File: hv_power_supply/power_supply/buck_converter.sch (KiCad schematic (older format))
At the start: 9 parts, among them U1 TLF50211ELXUMA2

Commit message: hvps buck rev2
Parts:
- removed C_IN1: C_47uF, footprints:C_0805_OEM, symbol formula:C_47uF
- removed C_OUT1: C_10uF, footprints:C_0805_OEM, symbol formula:C_10uF
- removed DNP1, DNP2, DNP3: R_0, symbol Device:R
- removed D_Schottky1: 10BQ100, symbol Device:D_Schottky
- removed L_OUT1: L_10uH, symbol Device:L
- removed R1: R_47k, symbol formula:R_47k
- removed U1: TLF50211ELXUMA2, symbol formula:TLF50211ELXUMA2
- added C1, C_IN: C_1uF, footprints:C_0805_OEM, symbol formula:C_1uF
- added C_OUT: C_10uF, footprints:C_0805_OEM, symbol formula:C_10uF
- added R?: R_10K, footprints:R_0805_OEM, symbol formula:R_10K
- added U2: MAXM15464, symbol formula:MAXM15464
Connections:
- net labels added: V_IN(24V), V_OUT(5V)
- net labels removed: VCC, VS
- wire segments 36 -> 22
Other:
- note removed: "Input Cap 2"
- note removed: "Input Cap 3\n"
- note removed: "Input Inductor"

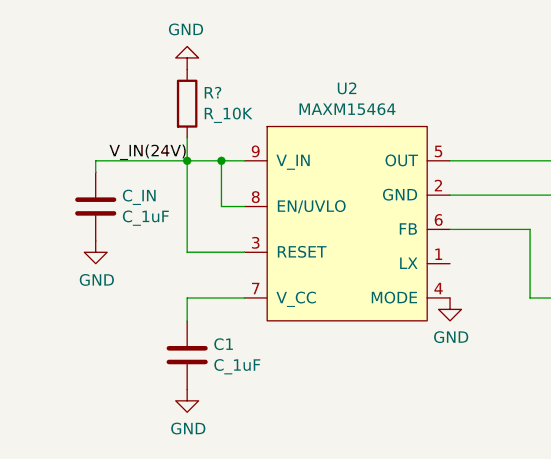
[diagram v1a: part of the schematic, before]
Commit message: buck with DNP part
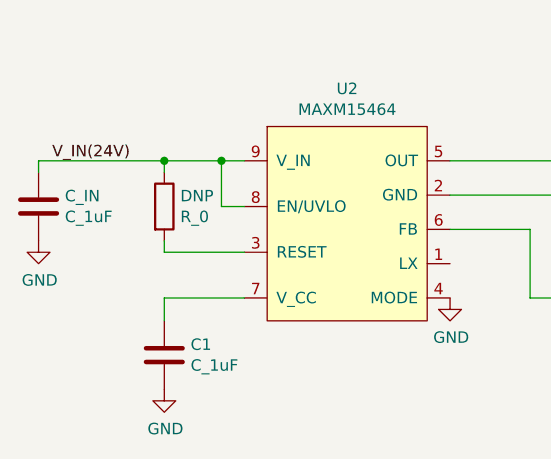
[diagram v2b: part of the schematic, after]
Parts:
- removed R?: R_10K, footprints:R_0805_OEM, symbol formula:R_10K
- added DNP: R_0, footprints:R_0603_1608Metric, symbol formula:R_0
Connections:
- net V_IN(24V): now also DNP.1; no longer U2.3 (RESET)
- new net: DNP.2, U2.3 (RESET)
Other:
- moved on the sheet: C1, C_IN
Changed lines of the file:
@@
 L formula:C_1uF C_IN
 U 1 1 60344498
-P 3700 3300
-F 0 "C_IN" H 3815 3396 50  0000 L CNN
-F 1 "C_1uF" H 3815 3305 50  0000 L CNN
-F 2 "footprints:C_0805_OEM" H 3738 3900 50  0001 C CNN
-F 3 "https://www.yageo.com/upload/media/product/productsearch/datasheet/mlcc/UPY-GPHC_Y5V_6.3V-to-50V_9.pdf" H 3725 4150 50  0001 C CNN
-F 4 "https://www.digikey.com/product-detail/en/yageo/CC0805ZKY5V9BB105/311-1909-1-ND/5195811#images" H 4125 3800 60  0001 C CNN "PurchasingLink"
-	1    3700 3300
+P 3450 3300
+F 0 "C_IN" H 3565 3396 50  0000 L CNN
+F 1 "C_1uF" H 3565 3305 50  0000 L CNN
+F 2 "footprints:C_0805_OEM" H 3488 3900 50  0001 C CNN
+F 3 "https://www.yageo.com/upload/media/product/productsearch/datasheet/mlcc/UPY-GPHC_Y5V_6.3V-to-50V_9.pdf" H 3475 4150 50  0001 C CNN
+F 4 "https://www.digikey.com/product-detail/en/yageo/CC0805ZKY5V9BB105/311-1909-1-ND/5195811#images" H 3875 3800 60  0001 C CNN "PurchasingLink"
+	1    3450 3300
 	1    0    0    -1
 $EndComp
@@
 L formula:C_1uF C1
 U 1 1 60347394
-P 4100 3950
-F 0 "C1" H 4215 4046 50  0000 L CNN
-F 1 "C_1uF" H 4215 3955 50  0000 L CNN
-F 2 "footprints:C_0805_OEM" H 4138 4550 50  0001 C CNN
-F 3 "https://www.yageo.com/upload/media/product/productsearch/datasheet/mlcc/UPY-GPHC_Y5V_6.3V-to-50V_9.pdf" H 4125 4800 50  0001 C CNN
-F 4 "https://www.digikey.com/product-detail/en/yageo/CC0805ZKY5V9BB105/311-1909-1-ND/5195811#images" H 4525 4450 60  0001 C CNN "PurchasingLink"
-	1    4100 3950
+P 4000 3950
+F 0 "C1" H 4115 4046 50  0000 L CNN
+F 1 "C_1uF" H 4115 3955 50  0000 L CNN
+F 2 "footprints:C_0805_OEM" H 4038 4550 50  0001 C CNN
+F 3 "https://www.yageo.com/upload/media/product/productsearch/datasheet/mlcc/UPY-GPHC_Y5V_6.3V-to-50V_9.pdf" H 4025 4800 50  0001 C CNN
+F 4 "https://www.digikey.com/product-detail/en/yageo/CC0805ZKY5V9BB105/311-1909-1-ND/5195811#images" H 4425 4450 60  0001 C CNN "PurchasingLink"
+	1    4000 3950
 	1    0    0    -1
 $EndComp
-Wire Wire Line
-	4100 3650 4100 3750
 $Comp
 L power:GND #PWR?
 U 1 1 6034E7B2
-P 4100 4050
-F 0 "#PWR?" H 4100 3800 50  0001 C CNN
-F 1 "GND" H 4105 3877 50  0000 C CNN
-F 2 "" H 4100 4050 50  0001 C CNN
-F 3 "" H 4100 4050 50  0001 C CNN
-	1    4100 4050
+P 4000 4050
+F 0 "#PWR?" H 4000 3800 50  0001 C CNN
+F 1 "GND" H 4005 3877 50  0000 C CNN
+F 2 "" H 4000 4050 50  0001 C CNN
+F 3 "" H 4000 4050 50  0001 C CNN
+	1    4000 4050
 	1    0    0    -1
 $EndComp
@@
 L power:GND #PWR?
 U 1 1 60350117
-P 3700 3400
-F 0 "#PWR?" H 3700 3150 50  0001 C CNN
-F 1 "GND" H 3705 3227 50  0000 C CNN
-F 2 "" H 3700 3400 50  0001 C CNN
-F 3 "" H 3700 3400 50  0001 C CNN
-	1    3700 3400
+P 3450 3400
+F 0 "#PWR?" H 3450 3150 50  0001 C CNN
+F 1 "GND" H 3455 3227 50  0000 C CNN
+F 2 "" H 3450 3400 50  0001 C CNN
+F 3 "" H 3450 3400 50  0001 C CNN
+	1    3450 3400
 	1    0    0    -1
 $EndComp
@@
 Text Label 6500 3050 0    50   ~ 0
 V_OUT(5V)
-Text Label 4100 3050 2    50   ~ 0
-V_IN(24V)
 Wire Wire Line
-	3700 3050 3700 3100
+	3450 3050 3450 3100
 $Comp
 L power:GND #PWR?
@@
 $EndComp
 Wire Wire Line
-	4100 3450 4100 3050
-Connection ~ 4100 3050
-Wire Wire Line
-	3700 3050 4100 3050
-Wire Wire Line
 	4350 3250 4250 3250
 Wire Wire Line
 	4250 3250 4250 3050
 Wire Wire Line
-	4100 3050 4250 3050
-Connection ~ 4250 3050
-Wire Wire Line
 	4250 3050 4350 3050
-Wire Wire Line
-	4100 3450 4350 3450
-Wire Wire Line
-	4100 3650 4350 3650
 Connection ~ 5850 3050
 Wire Wire Line
@@
 Wire Wire Line
 	5600 3650 6250 3650
+Text Label 3850 3050 2    50   ~ 0
+V_IN(24V)
 $Comp
-L formula:R_10K R?
-U 1 1 6039780D
-P 4100 2800
-F 0 "R?" H 4170 2846 50  0000 L CNN
-F 1 "R_10K" H 4170 2755 50  0000 L CNN
-F 2 "footprints:R_0805_OEM" H 4030 2800 50  0001 C CNN
-F 3 "http://www.bourns.com/data/global/pdfs/CRS.pdf" H 4180 2800 50  0001 C CNN
-F 4 "DK" H 4100 2800 60  0001 C CNN "MFN"
-F 5 "CRS0805-FX-1002ELFCT-ND" H 4100 2800 60  0001 C CNN "MPN"
-F 6 "https://www.digikey.com/products/en?keywords=CRS0805-FX-1002ELFCT-ND" H 4580 3200 60  0001 C CNN "PurchasingLink"
-	1    4100 2800
+L formula:R_0 DNP
+U 1 1 6040106D
+P 4000 3250
+F 0 "DNP" H 4070 3296 50  0000 L CNN
+F 1 "R_0" H 4070 3205 50  0000 L CNN
+F 2 "footprints:R_0603_1608Metric" H 3930 3250 50  0001 C CNN
+F 3 "http://industrial.panasonic.com/www-cgi/jvcr13pz.cgi?E+PZ+3+AOA0001+ERJ3GEY0R00V+7+WW" H 4080 3250 50  0001 C CNN
+F 4 "DK" H 4000 3250 60  0001 C CNN "MFN"
+F 5 "P0.0GCT-ND" H 4000 3250 60  0001 C CNN "MPN"
+F 6 "https://www.digikey.com/product-detail/en/panasonic-electronic-components/ERJ-3GEY0R00V/P0.0GCT-ND/134711" H 4480 3650 60  0001 C CNN "PurchasingLink"
+	1    4000 3250
 	1    0    0    -1
 $EndComp
 Wire Wire Line
-	4100 3050 4100 2950
-$Comp
-L power:GND #PWR?
-U 1 1 6039F701
-P 4100 2650
-F 0 "#PWR?" H 4100 2400 50  0001 C CNN
-F 1 "GND" H 4105 2477 50  0000 C CNN
-F 2 "" H 4100 2650 50  0001 C CNN
-F 3 "" H 4100 2650 50  0001 C CNN
-	1    4100 2650
-	-1   0    0    1
-$EndComp
+	4000 3750 4000 3650
+Wire Wire Line
+	4000 3650 4350 3650
+Wire Wire Line
+	4000 3400 4000 3450
+Wire Wire Line
+	4000 3450 4350 3450
+Wire Wire Line
+	3450 3050 4000 3050
+Connection ~ 4250 3050
+Wire Wire Line
+	4000 3100 4000 3050
+Connection ~ 4000 3050
+Wire Wire Line
+	4000 3050 4250 3050
 $EndSCHEMATC

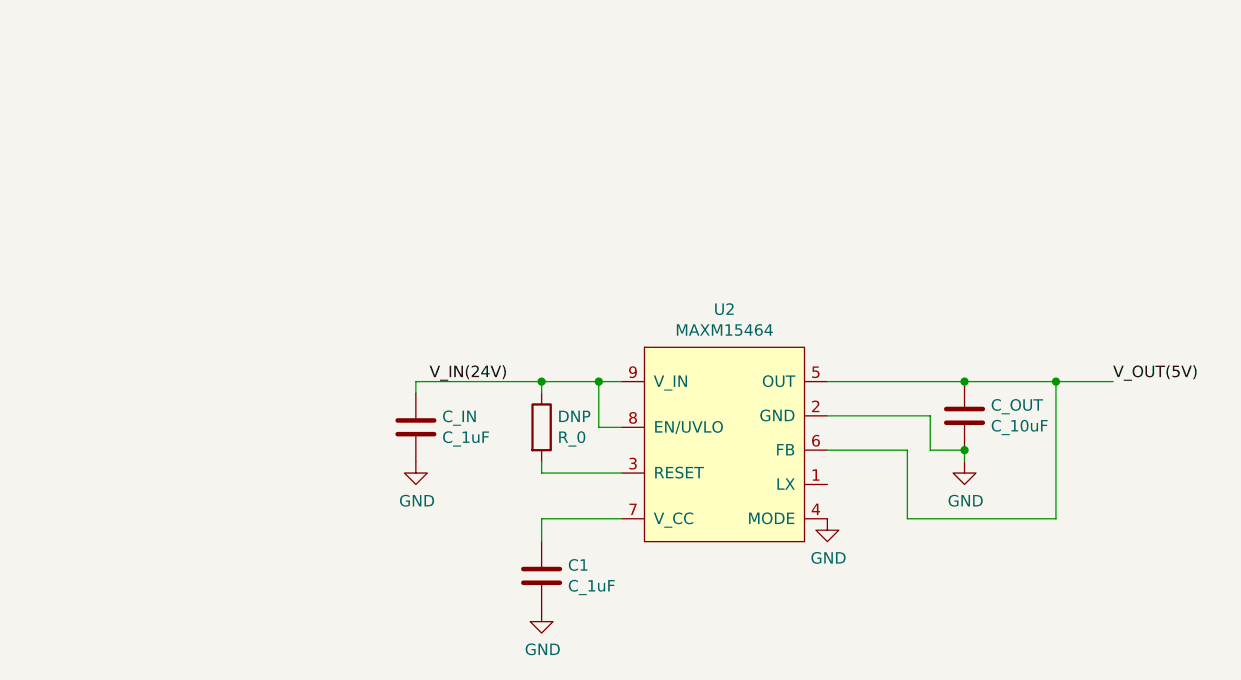
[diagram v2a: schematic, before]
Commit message: make schematic sheets talk to each other
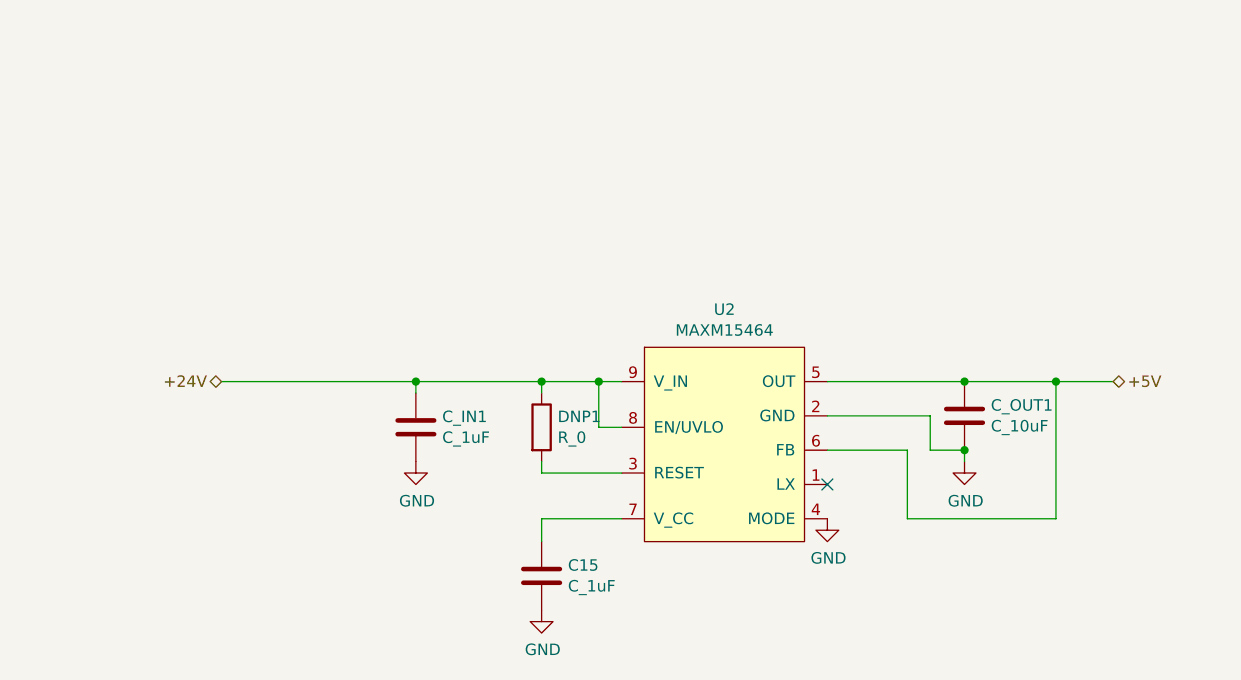
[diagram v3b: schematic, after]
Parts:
- renumbered C1 to C15, C_IN to C_IN1, C_OUT to C_OUT1, DNP to DNP1
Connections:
- net V_IN(24V) renamed +24V
- net V_OUT(5V) renamed +5V
- no-connect marks 0 -> 1
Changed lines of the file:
@@
 $Descr A4 11693 8268
 encoding utf-8
-Sheet 1 1
+Sheet 3 5
 Title ""
 Date ""
@@
 $EndComp
 $Comp
-L formula:C_1uF C_IN
+L formula:C_1uF C_IN1
 U 1 1 60344498
 P 3450 3300
-F 0 "C_IN" H 3565 3396 50  0000 L CNN
+F 0 "C_IN1" H 3565 3396 50  0000 L CNN
 F 1 "C_1uF" H 3565 3305 50  0000 L CNN
 F 2 "footprints:C_0805_OEM" H 3488 3900 50  0001 C CNN
@@
 $EndComp
 $Comp
-L formula:C_1uF C1
+L formula:C_1uF C15
 U 1 1 60347394
 P 4000 3950
-F 0 "C1" H 4115 4046 50  0000 L CNN
+F 0 "C15" H 4115 4046 50  0000 L CNN
 F 1 "C_1uF" H 4115 3955 50  0000 L CNN
 F 2 "footprints:C_0805_OEM" H 4038 4550 50  0001 C CNN
@@
 $EndComp
 $Comp
-L power:GND #PWR?
+L power:GND #PWR013
 U 1 1 6034E7B2
 P 4000 4050
-F 0 "#PWR?" H 4000 3800 50  0001 C CNN
+F 0 "#PWR013" H 4000 3800 50  0001 C CNN
 F 1 "GND" H 4005 3877 50  0000 C CNN
 F 2 "" H 4000 4050 50  0001 C CNN
@@
 $EndComp
 $Comp
-L power:GND #PWR?
+L power:GND #PWR012
 U 1 1 60350117
 P 3450 3400
-F 0 "#PWR?" H 3450 3150 50  0001 C CNN
+F 0 "#PWR012" H 3450 3150 50  0001 C CNN
 F 1 "GND" H 3455 3227 50  0000 C CNN
 F 2 "" H 3450 3400 50  0001 C CNN
@@
 $EndComp
 $Comp
-L power:GND #PWR?
+L power:GND #PWR015
 U 1 1 6034F654
 P 5850 3400
-F 0 "#PWR?" H 5850 3150 50  0001 C CNN
+F 0 "#PWR015" H 5850 3150 50  0001 C CNN
 F 1 "GND" H 5855 3227 50  0000 C CNN
 F 2 "" H 5850 3400 50  0001 C CNN
@@
 $EndComp
 $Comp
-L formula:C_10uF C_OUT
+L formula:C_10uF C_OUT1
 U 1 1 60345C25
 P 5850 3250
-F 0 "C_OUT" H 5965 3346 50  0000 L CNN
+F 0 "C_OUT1" H 5965 3346 50  0000 L CNN
 F 1 "C_10uF" H 5965 3255 50  0000 L CNN
 F 2 "footprints:C_0805_OEM" H 5888 3850 50  0001 C CNN
@@
 Wire Wire Line
 	6250 3650 6250 3050
-Text Label 6500 3050 0    50   ~ 0
-V_OUT(5V)
 Wire Wire Line
 	3450 3050 3450 3100
 $Comp
-L power:GND #PWR?
+L power:GND #PWR014
 U 1 1 6037D3E3
 P 5250 3650
-F 0 "#PWR?" H 5250 3400 50  0001 C CNN
+F 0 "#PWR014" H 5250 3400 50  0001 C CNN
 F 1 "GND" H 5255 3477 50  0000 C CNN
 F 2 "" H 5250 3650 50  0001 C CNN
@@
 Wire Wire Line
 	5600 3650 6250 3650
-Text Label 3850 3050 2    50   ~ 0
-V_IN(24V)
 $Comp
-L formula:R_0 DNP
+L formula:R_0 DNP1
 U 1 1 6040106D
 P 4000 3250
-F 0 "DNP" H 4070 3296 50  0000 L CNN
+F 0 "DNP1" H 4070 3296 50  0000 L CNN
 F 1 "R_0" H 4070 3205 50  0000 L CNN
 F 2 "footprints:R_0603_1608Metric" H 3930 3250 50  0001 C CNN
@@
 Wire Wire Line
 	4000 3050 4250 3050
+Text HLabel 6500 3050 2    50   BiDi ~ 0
++5V
+Wire Wire Line
+	3450 3050 2600 3050
+Connection ~ 3450 3050
+Text HLabel 2600 3050 0    50   BiDi ~ 0
++24V
+NoConn ~ 5250 3500
 $EndSCHEMATC

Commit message: Fixed all component footprint issues, beginning to lay out flyback portion
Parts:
- U2: footprint (none) -> footprints:MAXM15464; MPN (none) -> MAXM15464AMB+; Manufacturer (none) -> Maxim Integrated; Purchasing Link (none) -> https://www.digikey.com/en/products/detail/maxim-integrated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
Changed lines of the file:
@@
 $EndDescr
-$Comp
-L formula:MAXM15464 U2
-U 1 1 602D1F9A
-P 4800 3300
-F 0 "U2" H 4800 3865 50  0000 C CNN
-F 1 "MAXM15464" H 4800 3774 50  0000 C CNN
-F 2 "" H 4800 3900 50  0001 C CNN
-F 3 "" H 4800 3900 50  0001 C CNN
-	1    4800 3300
-	1    0    0    -1
-$EndComp
 $Comp
 L formula:C_1uF C_IN1
@@
 +24V
 NoConn ~ 5250 3500
+$Comp
+L formula:MAXM15464 U2
+U 1 1 6063BABC
+P 4800 3300
+F 0 "U2" H 4800 3865 50  0000 C CNN
+F 1 "MAXM15464" H 4800 3774 50  0000 C CNN
+F 2 "footprints:MAXM15464" H 4800 3900 50  0001 C CNN
+F 3 "https://media.digikey.com/pdf/Data%20Sheets/Maxim%20PDFs/MAXM15462-64_Rev4_10-26-18.pdf" H 4800 3900 50  0001 C CNN
+F 4 "https://www.digikey.com/en/products/detail/maxim-integrated/MAXM15464AMB/10209895" H 4800 3300 50  0001 C CNN "Purchasing Link"
+F 5 "Maxim Integrated" H 4800 3300 50  0001 C CNN "Manufacturer"
+F 6 "MAXM15464AMB+" H 4800 3300 50  0001 C CNN "MPN"
+	1    4800 3300
+	1    0    0    -1
+$EndComp
 $EndSCHEMATC
